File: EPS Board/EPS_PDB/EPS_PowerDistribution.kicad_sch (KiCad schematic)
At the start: 0 parts

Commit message: Modified EPS Power Distribution and Regulation Schematic
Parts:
- added 3.3V_Converter: LTC3624_3.3, EPS_Schematic_v2:SOP65P490X110-13N, symbol EPS_Schematic_v2-eagle-import:LTC3624_3.3
- added 5V_Converter: LTC3624_25, EPS_Schematic_v2:SOP65P490X110-13N, symbol EPS_Schematic_v2-eagle-import:LTC3624_25
- added ADCS_12V, ADCS_3.3V, ADCS_5V, COMM_5V, EPS_5V, OBC_5V: TPS259621DDAT, EPS_Schematic_v2:IC_TPS259621DDAT, symbol EPS_Schematic_v2-eagle-import:TPS259621DDAT
- added C1, C5: 10uF, Capacitor_SMD:C_0805_2012Metric_Pad1.18x1.45mm_HandSolder, symbol Device:C_Small
- added C2: 47uF, Capacitor_SMD:C_0805_2012Metric_Pad1.18x1.45mm_HandSolder, symbol Device:C_Small
- added C3, C6: 2.2uF, Capacitor_SMD:C_0805_2012Metric_Pad1.18x1.45mm_HandSolder, symbol Device:C_Small
- added C4: 4.7uF, Capacitor_SMD:C_0805_2012Metric_Pad1.18x1.45mm_HandSolder, symbol Device:C_Small
- added L1: 1.3uH, Inductor_SMD:L_0805_2012Metric_Pad1.15x1.40mm_HandSolder, symbol Device:L
- added L2: 16uH, Inductor_SMD:L_0805_2012Metric_Pad1.15x1.40mm_HandSolder, symbol Device:L
- added R1, R2, R4, R5: 400k, Resistor_SMD:R_0603_1608Metric_Pad0.98x0.95mm_HandSolder, symbol EPS_Schematic_v2-eagle-import:R-USCHIP-0805(2012-METRIC)
- added R10: 510, Resistor_SMD:R_0603_1608Metric_Pad0.98x0.95mm_HandSolder, symbol EPS_Schematic_v2-eagle-import:R-USCHIP-0805(2012-METRIC)
- added R11, R9: R-USCHIP-0805(2012-METRIC), Resistor_SMD:R_0603_1608Metric_Pad0.98x0.95mm_HandSolder, symbol EPS_Schematic_v2-eagle-import:R-USCHIP-0805(2012-METRIC)
- added R12, R8: 1.3k, Resistor_SMD:R_0603_1608Metric_Pad0.98x0.95mm_HandSolder, symbol EPS_Schematic_v2-eagle-import:R-USCHIP-0805(2012-METRIC)
- added R13: 2.2k, Resistor_SMD:R_0603_1608Metric_Pad0.98x0.95mm_HandSolder, symbol EPS_Schematic_v2-eagle-import:R-USCHIP-0805(2012-METRIC)
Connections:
- new net: OBC_5V.7 (ILM), R8.2
- new net: OBC_5V.8 (OVCSEL), R4.1
- new net: 5V_Converter.1 (SW), 5V_Converter.2 (SW2), L1.2
- new net: 5V_Converter.3 (VIN), 5V_Converter.4 (VIN2), 5V_Converter.5 (RUN), C1.2
- new net: 5V_Converter.9 (INTVCC), C3.2
- new net: ADCS_5V.7 (ILM), R9.2
- new net: COMM_5V.8 (OVCSEL), R5.1
- new net: ADCS_5V.8 (OVCSEL), R2.1
- new net: 3.3V_Converter.1 (SW), 3.3V_Converter.2 (SW2), L2.2
- new net: ADCS_12V.7 (ILM), R11.2
- new net: ADCS_3.3V.7 (ILM), R13.2
- new net: 3.3V_Converter.9 (INTVCC), C6.2
- new net: EPS_5V.7 (ILM), R10.2
- new net: EPS_5V.8 (OVCSEL), R1.1
- new net: 3.3V_Converter.3 (VIN), 3.3V_Converter.4 (VIN2), 3.3V_Converter.5 (RUN), C5.2
- new net: COMM_5V.7 (ILM), R12.2
- new net 12V_bus: ADCS_12V.4 (IN)
- new net 3.3V_PGOOD: 3.3V_Converter.6 (PGOOD)
- new net 3.3V_bus: 3.3V_Converter.8 (FB), ADCS_3.3V.4 (IN), C4.1, L2.1
- new net 5V_PGOOD: 5V_Converter.6 (PGOOD)
- new net 5V_bus: 5V_Converter.8 (FB), ADCS_5V.4 (IN), C2.1, COMM_5V.4 (IN), EPS_5V.4 (IN), L1.1, OBC_5V.4 (IN)
- new net ADCS_12V: ADCS_12V.5 (OUT)
- new net ADCS_12V_EN: ADCS_12V.3 (EN/UVLO)
- new net ADCS_12V_FLT: ADCS_12V.6 (~{FLT})
- new net ADCS_3.3V: ADCS_3.3V.5 (OUT)
- new net ADCS_3.3V_EN: ADCS_3.3V.3 (EN/UVLO)
- new net ADCS_3.3V_FLT: ADCS_3.3V.6 (~{FLT})
- new net ADCS_5V: ADCS_5V.5 (OUT)
- new net ADCS_5V_EN: ADCS_5V.3 (EN/UVLO)
- new net ADCS_5V_FLT: ADCS_5V.6 (~{FLT})
- new net COMM_5V: COMM_5V.5 (OUT)
- new net COMM_5V_EN: COMM_5V.3 (EN/UVLO)
- new net COMM_5V_FLT: COMM_5V.6 (~{FLT})
- new net EPS_5V: EPS_5V.5 (OUT)
- new net EPS_5V_EN: EPS_5V.3 (EN/UVLO)
- new net EPS_5V_FLT: EPS_5V.6 (~{FLT})
- new net GND: 3.3V_Converter.11 (GND), 3.3V_Converter.12 (GND2), 3.3V_Converter.13 (GND3), 5V_Converter.11 (GND), 5V_Converter.12 (GND2), 5V_Converter.13 (GND3), ADCS_12V.1 (GND), ADCS_12V.9 (EXP), ADCS_3.3V.1 (GND), ADCS_3.3V.8 (OVCSEL), ADCS_3.3V.9 (EXP), ADCS_5V.1 (GND), ADCS_5V.9 (EXP), C1.1, C2.2, C3.1, C4.2, C5.1, C6.1, COMM_5V.1 (GND), COMM_5V.9 (EXP), EPS_5V.1 (GND), EPS_5V.9 (EXP), OBC_5V.1 (GND), OBC_5V.9 (EXP), R1.2, R10.1, R11.1, R12.1, R13.1, R2.2, R4.2, R5.2, R8.1, R9.1
- new net OBC_5V: OBC_5V.5 (OUT)
- new net OBC_5V_EN: OBC_5V.3 (EN/UVLO)
- new net OBC_5V_FLT: OBC_5V.6 (~{FLT})
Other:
- note added: "CURRENT LIMITER"
- note added: "EPS DISTRIBUTION & REGULATION UNIT"
- note added: "VOLTAGE CONVERTER/REGULATOR"

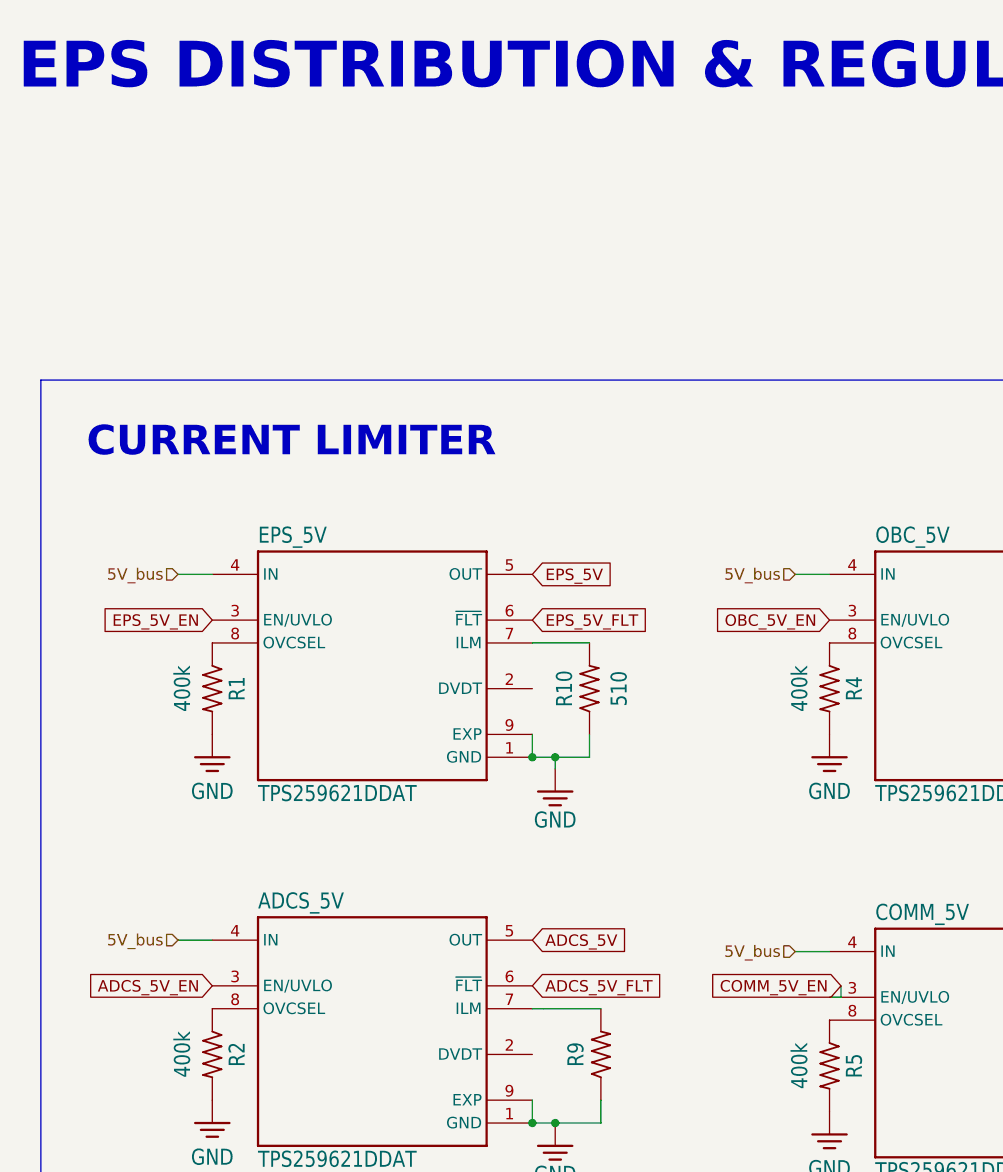
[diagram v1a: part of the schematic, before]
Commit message: Updated Schematic page settings
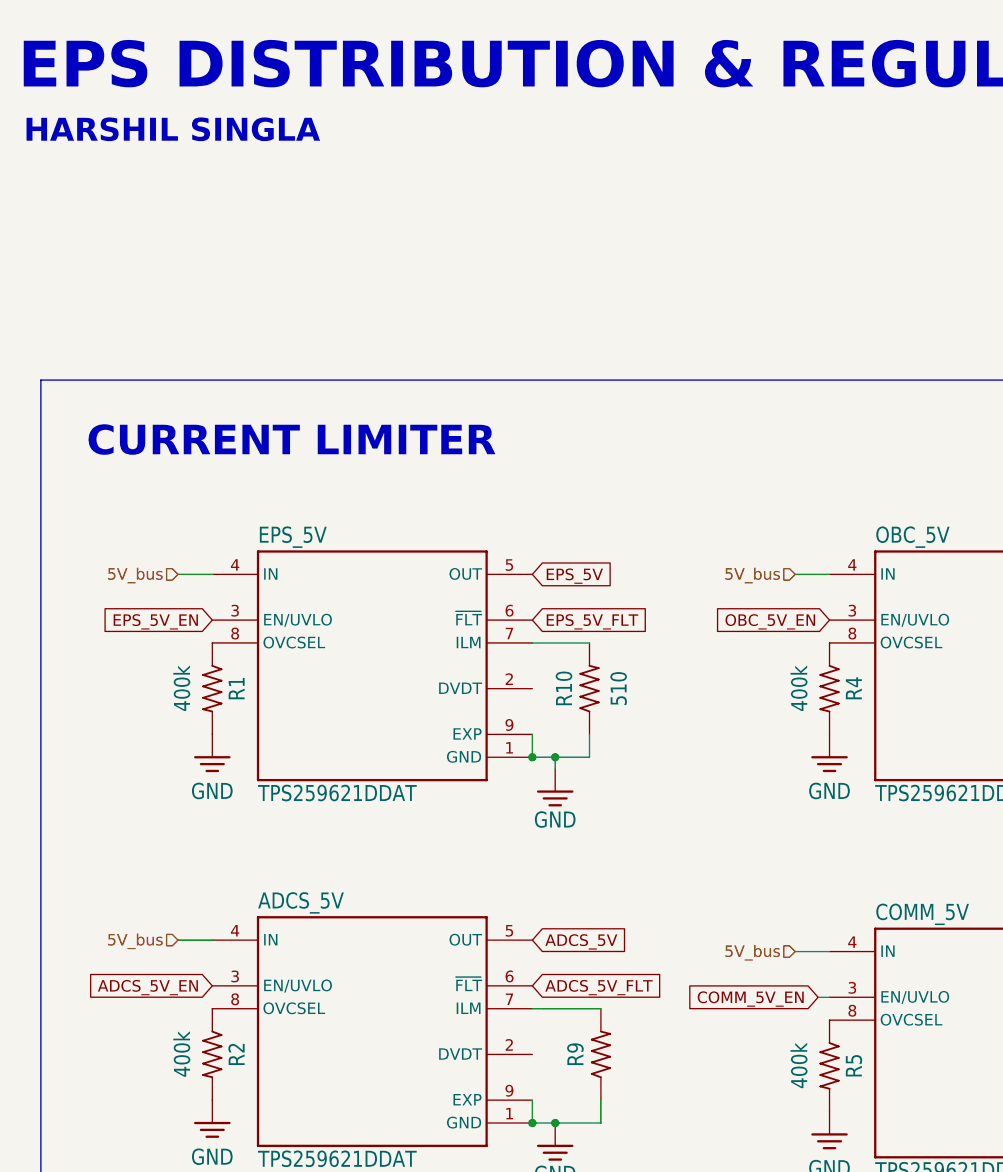
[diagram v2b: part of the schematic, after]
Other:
- note added: "HARSHIL SINGLA"
- company: (none) -> IIT Bombay Student Satellite Program
- title: (none) -> EPS Distribution and Regulation Unit
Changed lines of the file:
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@@
 (kicad_sch (version 20230121) (generator eeschema)
   (paper "A4")
+  (title_block
+    (title "EPS Distribution and Regulation Unit")
+    (date "2024-09-05")
+    (company "IIT Bombay Student Satellite Program")
+    (comment 1 "Author: Harshil Singla")
+  )
   (junction (at 74.93 180.34) (diameter 0) (color 0 0 0 0)
   )
@@
     (stroke (width 0) (type default))
   )
-  (wire (pts (xy 110.49 125.73) (xy 110.49 127))
-    (stroke (width 0) (type default))
-  )
   (wire (pts (xy 76.2 140.97) (xy 78.74 140.97))
     (stroke (width 0.1524) (type solid))
@@
     (stroke (width 0) (type default))
   )
-  (wire (pts (xy 110.49 127) (xy 109.22 127))
+  (wire (pts (xy 107.95 127) (xy 109.22 127))
     (stroke (width 0) (type default))
   )
@@
     (effects (font (size 3.27 3.27) (thickness 0.654) bold) (justify left bottom))
   )
-  (global_label "COMM_5V_EN" (shape input) (at 110.49 125.73 180) (fields_autoplaced)
+  (text "HARSHIL SINGLA" (at 19.685 32.385 0)
+    (effects (font (size 2.54 2.54) bold) (justify left bottom))
+  )
+  (global_label "COMM_5V_EN" (shape input) (at 107.95 127 180) (fields_autoplaced)
     (effects (font (size 1.27 1.27)) (justify right))
-    (property "Intersheetrefs" "${INTERSHEET_REFS}" (at 95.2887 125.73 0)
+    (property "Intersheetrefs" "${INTERSHEET_REFS}" (at 92.7487 127 0)
       (effects (font (size 1.27 1.27)) (justify right) hide)
     )
@@
     )
     (pin "1")
+    (pin "2")
+    (pin "3")
+    (pin "4")
+    (pin "5")
+    (pin "6")
     (pin "7")
-    (pin "2")
-    (pin "3")
-    (pin "6")
-    (pin "4")
     (pin "8")
     (pin "9")
-    (pin "5")
     (instances
       (project "EPS_PDB"
@@
       (effects (font (size 1.27 1.27)) hide)
     )
+    (pin "1")
+    (pin "10")
+    (pin "11")
+    (pin "12")
+    (pin "13")
+    (pin "2")
+    (pin "3")
+    (pin "4")
+    (pin "5")
+    (pin "6")
+    (pin "7")
+    (pin "8")
     (pin "9")
-    (pin "1")
-    (pin "4")
-    (pin "2")
-    (pin "8")
-    (pin "6")
-    (pin "10")
-    (pin "3")
-    (pin "12")
-    (pin "11")
-    (pin "13")
-    (pin "5")
-    (pin "7")
     (instances
       (project "EPS_PDB"
@@
       (effects (font (size 1.27 1.27)) hide)
     )
-    (pin "2")
-    (pin "1")
+    (pin "1")
+    (pin "2")
     (instances
       (project "EPS_PDB"
@@
       (effects (font (size 1.27 1.27)) hide)
     )
-    (pin "2")
-    (pin "1")
+    (pin "1")
+    (pin "2")
     (instances
       (project "EPS_PDB"
@@
       (effects (font (size 1.27 1.27)) hide)
     )
-    (pin "2")
-    (pin "1")
+    (pin "1")
+    (pin "2")
     (instances
       (project "EPS_PDB"
@@
       (effects (font (size 1.27 1.27)) hide)
     )
-    (pin "2")
-    (pin "1")
+    (pin "1")
+    (pin "2")
     (instances
       (project "EPS_PDB"
@@
     )
     (pin "1")
-    (pin "7")
-    (pin "9")
-    (pin "2")
-    (pin "6")
-    (pin "8")
+    (pin "2")
     (pin "3")
     (pin "4")
     (pin "5")
+    (pin "6")
+    (pin "7")
+    (pin "8")
+    (pin "9")
     (instances
       (project "EPS_PDB"
@@
       (effects (font (size 1.27 1.27)) hide)
     )
-    (pin "2")
-    (pin "1")
+    (pin "1")
+    (pin "2")
     (instances
       (project "EPS_PDB"
@@
       (effects (font (size 1.27 1.27)) hide)
     )
-    (pin "2")
-    (pin "1")
+    (pin "1")
+    (pin "2")
     (instances
       (project "EPS_PDB"
@@
       (effects (font (size 1.27 1.27)) hide)
     )
-    (pin "2")
-    (pin "1")
+    (pin "1")
+    (pin "2")
     (instances
       (project "EPS_PDB"
@@
       (effects (font (size 1.27 1.27)) hide)
     )
-    (pin "2")
-    (pin "1")
+    (pin "1")
+    (pin "2")
     (instances
       (project "EPS_PDB"
@@
     )
     (pin "1")
-    (pin "3")
-    (pin "2")
-    (pin "4")
-    (pin "6")
-    (pin "8")
-    (pin "5")
-    (pin "7")
-    (pin "9")
-    (instances
-      (project "EPS_PDB"
-        (path "/b6081578-ab04-44e2-a71a-4911a5b750e4/2d9f4680-6d7b-4671-a50c-25972cd78742"
-          (reference "ADCS_12V") (unit 1)
-        )
-      )
-    )
-  )
-  (symbol (lib_id "EPS_Schematic_v2-eagle-import:TPS259621DDAT") (at 127 170.18 0) (unit 1)
-    (in_bom yes) (on_board yes) (dnp no)
-    (property "Reference" "ADCS_3.3V" (at 114.3 156.718 0)
-      (effects (font (size 1.778 1.5113)) (justify left bottom))
-    )
-    (property "Value" "TPS259621DDAT" (at 114.3 185.42 0)
-      (effects (font (size 1.778 1.5113)) (justify left bottom))
-    )
-    (property "Footprint" "EPS_Schematic_v2:IC_TPS259621DDAT" (at 127 170.18 0)
-      (effects (font (size 1.27 1.27)) hide)
-    )
-    (property "Datasheet" "" (at 127 170.18 0)
-      (effects (font (size 1.27 1.27)) hide)
-    )
-    (pin "1")
+    (pin "2")
     (pin "3")
     (pin "4")
     (pin "5")
+    (pin "6")
     (pin "7")
-    (pin "2")
+    (pin "8")
     (pin "9")
+    (instances
+      (project "EPS_PDB"
+        (path "/b6081578-ab04-44e2-a71a-4911a5b750e4/2d9f4680-6d7b-4671-a50c-25972cd78742"
+          (reference "ADCS_12V") (unit 1)
+        )
+      )
+    )
+  )
+  (symbol (lib_id "EPS_Schematic_v2-eagle-import:TPS259621DDAT") (at 127 170.18 0) (unit 1)
+    (in_bom yes) (on_board yes) (dnp no)
+    (property "Reference" "ADCS_3.3V" (at 114.3 156.718 0)
+      (effects (font (size 1.778 1.5113)) (justify left bottom))
+    )
+    (property "Value" "TPS259621DDAT" (at 114.3 185.42 0)
+      (effects (font (size 1.778 1.5113)) (justify left bottom))
+    )
+    (property "Footprint" "EPS_Schematic_v2:IC_TPS259621DDAT" (at 127 170.18 0)
+      (effects (font (size 1.27 1.27)) hide)
+    )
+    (property "Datasheet" "" (at 127 170.18 0)
+      (effects (font (size 1.27 1.27)) hide)
+    )
+    (pin "1")
+    (pin "2")
+    (pin "3")
+    (pin "4")
+    (pin "5")
     (pin "6")
+    (pin "7")
     (pin "8")
+    (pin "9")
     (instances
       (project "EPS_PDB"
@@
       (effects (font (size 1.27 1.27)) hide)
     )
-    (pin "2")
-    (pin "1")
+    (pin "1")
+    (pin "2")
     (instances
       (project "EPS_PDB"
@@
       (effects (font (size 1.27 1.27)) hide)
     )
-    (pin "2")
-    (pin "1")
+    (pin "1")
+    (pin "2")
     (instances
       (project "EPS_PDB"
@@
       (effects (font (size 1.27 1.27)) hide)
     )
-    (pin "2")
-    (pin "1")
+    (pin "1")
+    (pin "2")
     (instances
       (project "EPS_PDB"
@@
       (effects (font (size 1.27 1.27)) hide)
     )
-    (pin "2")
-    (pin "1")
+    (pin "1")
+    (pin "2")
     (instances
       (project "EPS_PDB"
@@
       (effects (font (size 1.27 1.27)) hide)
     )
+    (pin "1")
+    (pin "2")
+    (pin "3")
     (pin "4")
-    (pin "2")
-    (pin "3")
-    (pin "1")
     (pin "5")
     (pin "6")
+    (pin "7")
     (pin "8")
     (pin "9")
-    (pin "7")
     (instances
       (project "EPS_PDB"
@@
       (effects (font (size 1.27 1.27)) hide)
     )
-    (pin "2")
-    (pin "1")
+    (pin "1")
+    (pin "2")
     (instances
       (project "EPS_PDB"
@@
       (effects (font (size 1.27 1.27)) hide)
     )
-    (pin "2")
-    (pin "1")
+    (pin "1")
+    (pin "2")
     (instances
       (project "EPS_PDB"
@@
       (effects (font (size 1.27 1.27)) hide)
     )
-    (pin "2")
-    (pin "1")
+    (pin "1")
+    (pin "2")
     (instances
       (project "EPS_PDB"
@@
       (effects (font (size 1.27 1.27)) hide)
     )
-    (pin "5")
-    (pin "1")
+    (pin "1")
+    (pin "10")
     (pin "11")
     (pin "12")
+    (pin "13")
+    (pin "2")
+    (pin "3")
+    (pin "4")
+    (pin "5")
     (pin "6")
+    (pin "7")
     (pin "8")
-    (pin "7")
-    (pin "13")
-    (pin "2")
-    (pin "3")
-    (pin "10")
     (pin "9")
-    (pin "4")
     (instances
       (project "EPS_PDB"
@@
       (effects (font (size 1.27 1.27)) hide)
     )
-    (pin "2")
-    (pin "1")
+    (pin "1")
+    (pin "2")
     (instances
       (project "EPS_PDB"
@@
     )
     (pin "1")
+    (pin "2")
+    (pin "3")
+    (pin "4")
+    (pin "5")
+    (pin "6")
     (pin "7")
-    (pin "6")
     (pin "8")
-    (pin "5")
-    (pin "2")
-    (pin "3")
     (pin "9")
-    (pin "4")
     (instances
       (project "EPS_PDB"
@@
       (effects (font (size 1.27 1.27)) hide)
     )
-    (pin "2")
-    (pin "1")
+    (pin "1")
+    (pin "2")
     (instances
       (project "EPS_PDB"
@@
       (effects (font (size 1.27 1.27)) hide)
     )
-    (pin "2")
-    (pin "1")
-    (instances
-      (project "EPS_PDB"
+    (pin "1")
+    (pin "2")
+    (instances
+      (project "EPS_PDB"

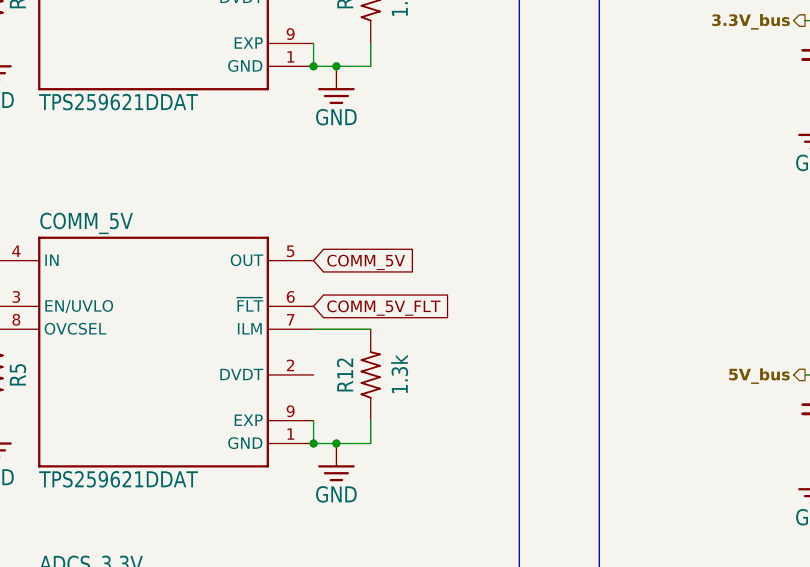
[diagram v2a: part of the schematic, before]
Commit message: EPS PDB Board Schematic progress
Interfaces defined in EPS PDB board Schematic
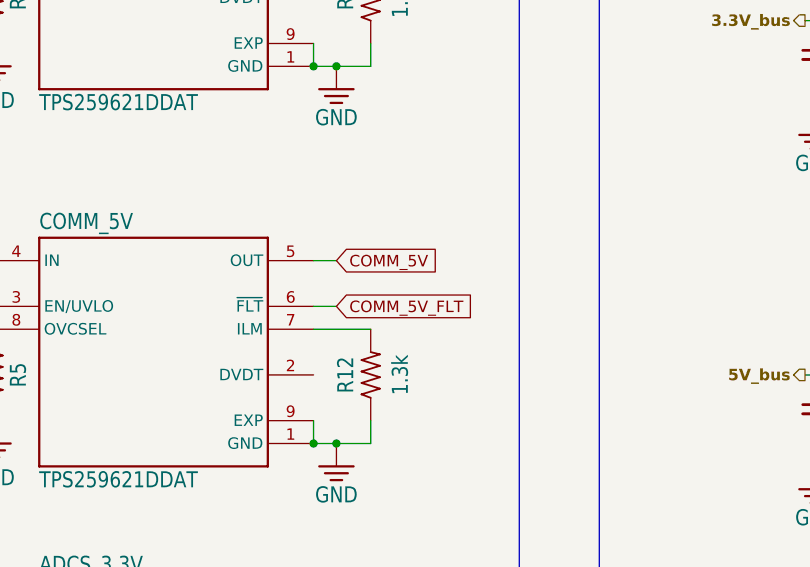
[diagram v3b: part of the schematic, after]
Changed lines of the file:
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@@
+    (stroke (width 0) (type default))
+  )
+  (wire (pts (xy 147.32 127) (xy 144.78 127))
     (stroke (width 0) (type default))
   )
@@
   (wire (pts (xy 149.86 180.34) (xy 149.86 182.88))
     (stroke (width 0.1524) (type solid))
+  )
+  (wire (pts (xy 147.32 121.92) (xy 144.78 121.92))
+    (stroke (width 0) (type default))
   )
   (wire (pts (xy 36.83 80.01) (xy 40.64 80.01))
@@
     )
   )
-  (global_label "COMM_5V" (shape input) (at 144.78 121.92 0) (fields_autoplaced)
-    (effects (font (size 1.27 1.27)) (justify left))
-    (property "Intersheetrefs" "${INTERSHEET_REFS}" (at 156.5342 121.92 0)
+  (global_label "COMM_5V" (shape input) (at 147.32 121.92 0) (fields_autoplaced)
+    (effects (font (size 1.27 1.27)) (justify left))
+    (property "Intersheetrefs" "${INTERSHEET_REFS}" (at 159.0742 121.92 0)
       (effects (font (size 1.27 1.27)) (justify left) hide)
     )
@@
     )
   )
-  (global_label "COMM_5V_FLT" (shape input) (at 144.78 127 0) (fields_autoplaced)
-    (effects (font (size 1.27 1.27)) (justify left))
-    (property "Intersheetrefs" "${INTERSHEET_REFS}" (at 160.5861 127 0)
-      (effects (font (size 1.27 1.27)) (justify left) hide)
-    )
+  (global_label "COMM_5V_FLT" (shape input) (at 147.32 127 0) (fields_autoplaced)
+    (effects (font (size 1.27 1.27)) (justify left))
+    (property "Intersheetrefs" "${INTERSHEET_REFS}" (at 163.1261 127 0)
+      (effects (font (size 1.27 1.27)) (justify left) hide)
+    )
